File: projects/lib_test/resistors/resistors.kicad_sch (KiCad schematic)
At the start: 0 parts

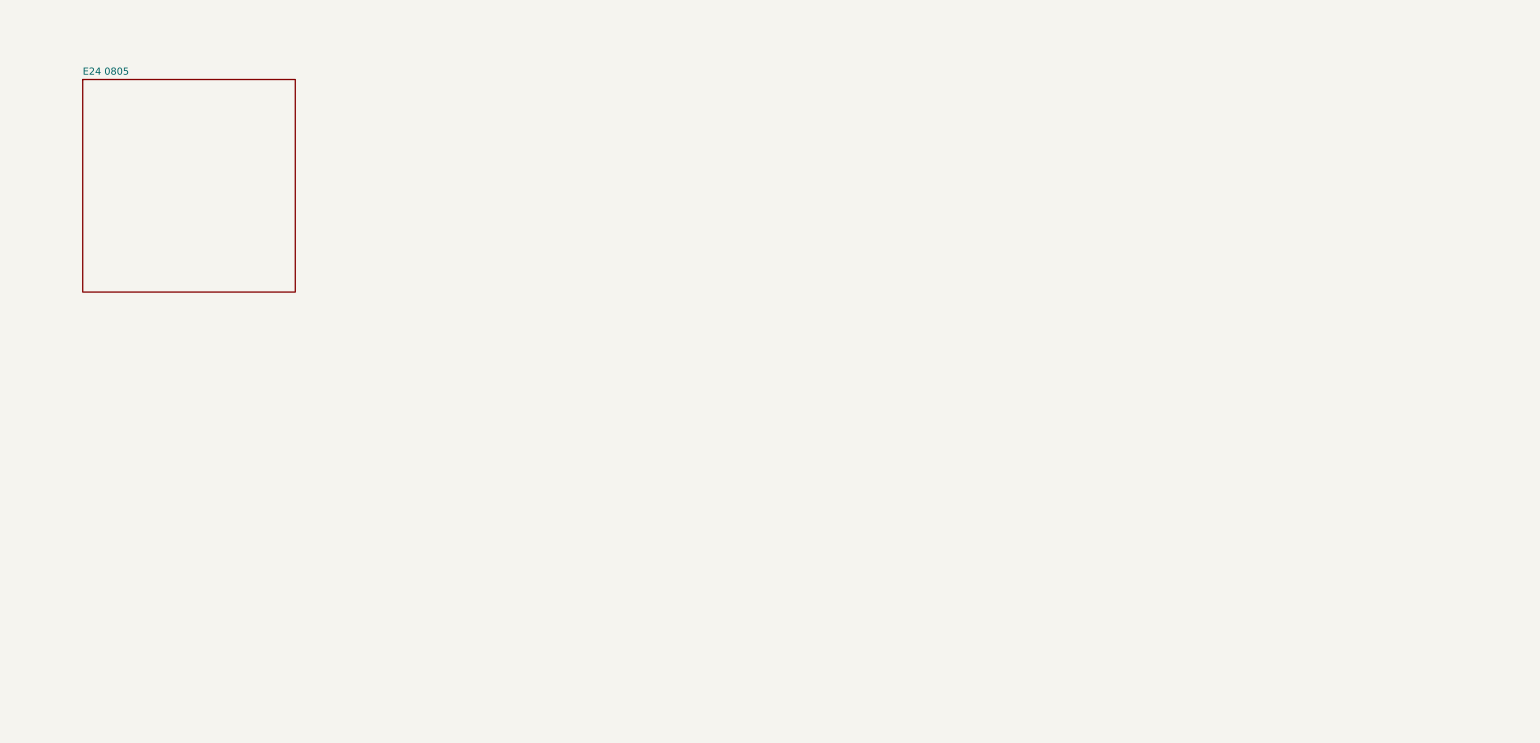
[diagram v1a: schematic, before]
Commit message: put all symbols in the test designs
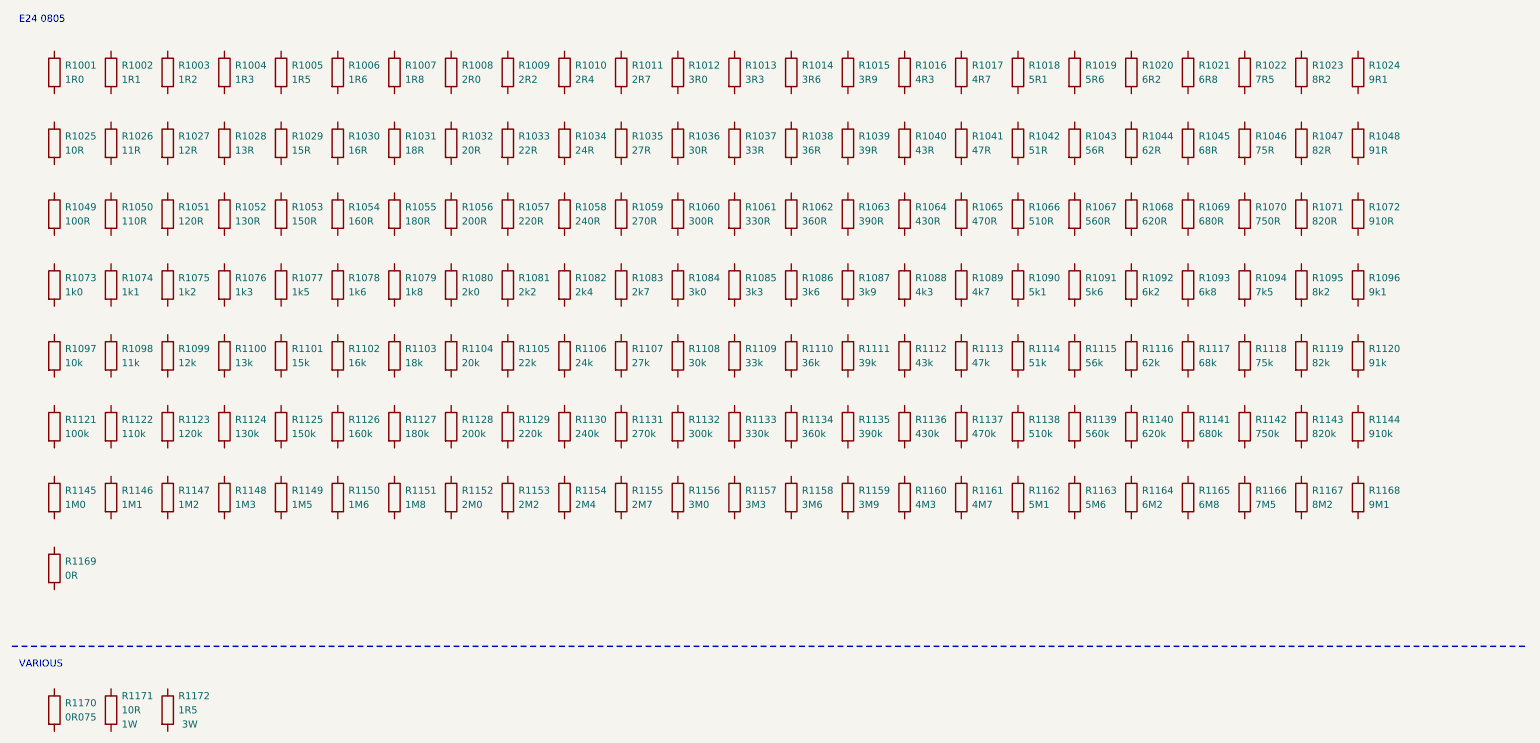
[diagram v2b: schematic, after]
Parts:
- added R1001: 1R0, lily_footprints:res_0805, symbol lily_symbols:res_1R0_1%_125mW_0805
- added R1002: 1R1, lily_footprints:res_0805, symbol lily_symbols:res_1R1_1%_125mW_0805
- added R1003: 1R2, lily_footprints:res_0805, symbol lily_symbols:res_1R2_1%_125mW_0805
- added R1004: 1R3, lily_footprints:res_0805, symbol lily_symbols:res_1R3_1%_125mW_0805
- added R1005: 1R5, lily_footprints:res_0805, symbol lily_symbols:res_1R5_1%_125mW_0805
- added R1006: 1R6, lily_footprints:res_0805, symbol lily_symbols:res_1R6_1%_125mW_0805
- added R1007: 1R8, lily_footprints:res_0805, symbol lily_symbols:res_1R8_1%_125mW_0805
- added R1008: 2R0, lily_footprints:res_0805, symbol lily_symbols:res_2R0_1%_125mW_0805
- added R1009: 2R2, lily_footprints:res_0805, symbol lily_symbols:res_2R2_1%_125mW_0805
- added R1010: 2R4, lily_footprints:res_0805, symbol lily_symbols:res_2R4_1%_125mW_0805
- added R1011: 2R7, lily_footprints:res_0805, symbol lily_symbols:res_2R7_1%_125mW_0805
- added R1012: 3R0, lily_footprints:res_0805, symbol lily_symbols:res_3R0_1%_125mW_0805
- added R1013: 3R3, lily_footprints:res_0805, symbol lily_symbols:res_3R3_1%_125mW_0805
- added R1014: 3R6, lily_footprints:res_0805, symbol lily_symbols:res_3R6_1%_125mW_0805
- added R1015: 3R9, lily_footprints:res_0805, symbol lily_symbols:res_3R9_1%_125mW_0805
- added R1016: 4R3, lily_footprints:res_0805, symbol lily_symbols:res_4R3_1%_125mW_0805
- added R1017: 4R7, lily_footprints:res_0805, symbol lily_symbols:res_4R7_1%_125mW_0805
- added R1018: 5R1, lily_footprints:res_0805, symbol lily_symbols:res_5R1_1%_125mW_0805
- added R1019: 5R6, lily_footprints:res_0805, symbol lily_symbols:res_5R6_1%_125mW_0805
- added R1020: 6R2, lily_footprints:res_0805, symbol lily_symbols:res_6R2_1%_125mW_0805
- added R1021: 6R8, lily_footprints:res_0805, symbol lily_symbols:res_6R8_1%_125mW_0805
- added R1022: 7R5, lily_footprints:res_0805, symbol lily_symbols:res_7R5_1%_125mW_0805
- added R1023: 8R2, lily_footprints:res_0805, symbol lily_symbols:res_8R2_1%_125mW_0805
- added R1024: 9R1, lily_footprints:res_0805, symbol lily_symbols:res_9R1_1%_125mW_0805
- added R1025: 10R, lily_footprints:res_0805, symbol lily_symbols:res_10R_1%_125mW_0805
- added R1026: 11R, lily_footprints:res_0805, symbol lily_symbols:res_11R_1%_125mW_0805
- added R1027: 12R, lily_footprints:res_0805, symbol lily_symbols:res_12R_1%_125mW_0805
- added R1028: 13R, lily_footprints:res_0805, symbol lily_symbols:res_13R_1%_125mW_0805
- added R1029: 15R, lily_footprints:res_0805, symbol lily_symbols:res_15R_1%_125mW_0805
- added R1030: 16R, lily_footprints:res_0805, symbol lily_symbols:res_16R_1%_125mW_0805
- added R1031: 18R, lily_footprints:res_0805, symbol lily_symbols:res_18R_1%_125mW_0805
- added R1032: 20R, lily_footprints:res_0805, symbol lily_symbols:res_20R_1%_125mW_0805
- added R1033: 22R, lily_footprints:res_0805, symbol lily_symbols:res_22R_1%_125mW_0805
- added R1034: 24R, lily_footprints:res_0805, symbol lily_symbols:res_24R_1%_125mW_0805
- added R1035: 27R, lily_footprints:res_0805, symbol lily_symbols:res_27R_1%_125mW_0805
- added R1036: 30R, lily_footprints:res_0805, symbol lily_symbols:res_30R_1%_125mW_0805
- added R1037: 33R, lily_footprints:res_0805, symbol lily_symbols:res_33R_1%_125mW_0805
- added R1038: 36R, lily_footprints:res_0805, symbol lily_symbols:res_36R_1%_125mW_0805
- added R1039: 39R, lily_footprints:res_0805, symbol lily_symbols:res_39R_1%_125mW_0805
- added R1040: 43R, lily_footprints:res_0805, symbol lily_symbols:res_43R_1%_125mW_0805
- added R1041: 47R, lily_footprints:res_0805, symbol lily_symbols:res_47R_1%_125mW_0805
- added R1042: 51R, lily_footprints:res_0805, symbol lily_symbols:res_51R_1%_125mW_0805
- added R1043: 56R, lily_footprints:res_0805, symbol lily_symbols:res_56R_1%_125mW_0805
- added R1044: 62R, lily_footprints:res_0805, symbol lily_symbols:res_62R_1%_125mW_0805
- added R1045: 68R, lily_footprints:res_0805, symbol lily_symbols:res_68R_1%_125mW_0805
- added R1046: 75R, lily_footprints:res_0805, symbol lily_symbols:res_75R_1%_125mW_0805
- added R1047: 82R, lily_footprints:res_0805, symbol lily_symbols:res_82R_1%_125mW_0805
- added R1048: 91R, lily_footprints:res_0805, symbol lily_symbols:res_91R_1%_125mW_0805
- added R1049: 100R, lily_footprints:res_0805, symbol lily_symbols:res_100R_1%_125mW_0805
- added R1050: 110R, lily_footprints:res_0805, symbol lily_symbols:res_110R_1%_125mW_0805
- added R1051: 120R, lily_footprints:res_0805, symbol lily_symbols:res_120R_1%_125mW_0805
- added R1052: 130R, lily_footprints:res_0805, symbol lily_symbols:res_130R_1%_125mW_0805
- added R1053: 150R, lily_footprints:res_0805, symbol lily_symbols:res_150R_1%_125mW_0805
- added R1054: 160R, lily_footprints:res_0805, symbol lily_symbols:res_160R_1%_125mW_0805
- added R1055: 180R, lily_footprints:res_0805, symbol lily_symbols:res_180R_1%_125mW_0805
- added R1056: 200R, lily_footprints:res_0805, symbol lily_symbols:res_200R_1%_125mW_0805
- added R1057: 220R, lily_footprints:res_0805, symbol lily_symbols:res_220R_1%_125mW_0805
- added R1058: 240R, lily_footprints:res_0805, symbol lily_symbols:res_240R_1%_125mW_0805
- added R1059: 270R, lily_footprints:res_0805, symbol lily_symbols:res_270R_1%_125mW_0805
- added R1060: 300R, lily_footprints:res_0805, symbol lily_symbols:res_300R_1%_125mW_0805
- added R1061: 330R, lily_footprints:res_0805, symbol lily_symbols:res_330R_1%_125mW_0805
- added R1062: 360R, lily_footprints:res_0805, symbol lily_symbols:res_360R_1%_125mW_0805
- added R1063: 390R, lily_footprints:res_0805, symbol lily_symbols:res_390R_1%_125mW_0805
- added R1064: 430R, lily_footprints:res_0805, symbol lily_symbols:res_430R_1%_125mW_0805
- added R1065: 470R, lily_footprints:res_0805, symbol lily_symbols:res_470R_1%_125mW_0805
- added R1066: 510R, lily_footprints:res_0805, symbol lily_symbols:res_510R_1%_125mW_0805
- added R1067: 560R, lily_footprints:res_0805, symbol lily_symbols:res_560R_1%_125mW_0805
- added R1068: 620R, lily_footprints:res_0805, symbol lily_symbols:res_620R_1%_125mW_0805
- added R1069: 680R, lily_footprints:res_0805, symbol lily_symbols:res_680R_1%_125mW_0805
- added R1070: 750R, lily_footprints:res_0805, symbol lily_symbols:res_750R_1%_125mW_0805
- added R1071: 820R, lily_footprints:res_0805, symbol lily_symbols:res_820R_1%_125mW_0805
- added R1072: 910R, lily_footprints:res_0805, symbol lily_symbols:res_910R_1%_125mW_0805
- added R1073: 1k0, lily_footprints:res_0805, symbol lily_symbols:res_1k0_1%_125mW_0805
- added R1074: 1k1, lily_footprints:res_0805, symbol lily_symbols:res_1k1_1%_125mW_0805
- added R1075: 1k2, lily_footprints:res_0805, symbol lily_symbols:res_1k2_1%_125mW_0805
- added R1076: 1k3, lily_footprints:res_0805, symbol lily_symbols:res_1k3_1%_125mW_0805
- added R1077: 1k5, lily_footprints:res_0805, symbol lily_symbols:res_1k5_1%_125mW_0805
- added R1078: 1k6, lily_footprints:res_0805, symbol lily_symbols:res_1k6_1%_125mW_0805
- added R1079: 1k8, lily_footprints:res_0805, symbol lily_symbols:res_1k8_1%_125mW_0805
- added R1080: 2k0, lily_footprints:res_0805, symbol lily_symbols:res_2k0_1%_125mW_0805
- added R1081: 2k2, lily_footprints:res_0805, symbol lily_symbols:res_2k2_1%_125mW_0805
- added R1082: 2k4, lily_footprints:res_0805, symbol lily_symbols:res_2k4_1%_125mW_0805
- added R1083: 2k7, lily_footprints:res_0805, symbol lily_symbols:res_2k7_1%_125mW_0805
- added R1084: 3k0, lily_footprints:res_0805, symbol lily_symbols:res_3k0_1%_125mW_0805
- added R1085: 3k3, lily_footprints:res_0805, symbol lily_symbols:res_3k3_1%_125mW_0805
- added R1086: 3k6, lily_footprints:res_0805, symbol lily_symbols:res_3k6_1%_125mW_0805
- added R1087: 3k9, lily_footprints:res_0805, symbol lily_symbols:res_3k9_1%_125mW_0805
- added R1088: 4k3, lily_footprints:res_0805, symbol lily_symbols:res_4k3_1%_125mW_0805
- added R1089: 4k7, lily_footprints:res_0805, symbol lily_symbols:res_4k7_1%_125mW_0805
- added R1090: 5k1, lily_footprints:res_0805, symbol lily_symbols:res_5k1_1%_125mW_0805
- added R1091: 5k6, lily_footprints:res_0805, symbol lily_symbols:res_5k6_1%_125mW_0805
- added R1092: 6k2, lily_footprints:res_0805, symbol lily_symbols:res_6k2_1%_125mW_0805
- added R1093: 6k8, lily_footprints:res_0805, symbol lily_symbols:res_6k8_1%_125mW_0805
- added R1094: 7k5, lily_footprints:res_0805, symbol lily_symbols:res_7k5_1%_125mW_0805
- added R1095: 8k2, lily_footprints:res_0805, symbol lily_symbols:res_8k2_1%_125mW_0805
- added R1096: 9k1, lily_footprints:res_0805, symbol lily_symbols:res_9k1_1%_125mW_0805
- added R1097: 10k, lily_footprints:res_0805, symbol lily_symbols:res_10k_1%_125mW_0805
- added R1098: 11k, lily_footprints:res_0805, symbol lily_symbols:res_11k_1%_125mW_0805
- added R1099: 12k, lily_footprints:res_0805, symbol lily_symbols:res_12k_1%_125mW_0805
- added R1100: 13k, lily_footprints:res_0805, symbol lily_symbols:res_13k_1%_125mW_0805
- added R1101: 15k, lily_footprints:res_0805, symbol lily_symbols:res_15k_1%_125mW_0805
- added R1102: 16k, lily_footprints:res_0805, symbol lily_symbols:res_16k_1%_125mW_0805
- added R1103: 18k, lily_footprints:res_0805, symbol lily_symbols:res_18k_1%_125mW_0805
- added R1104: 20k, lily_footprints:res_0805, symbol lily_symbols:res_20k_1%_125mW_0805
- added R1105: 22k, lily_footprints:res_0805, symbol lily_symbols:res_22k_1%_125mW_0805
- added R1106: 24k, lily_footprints:res_0805, symbol lily_symbols:res_24k_1%_125mW_0805
- added R1107: 27k, lily_footprints:res_0805, symbol lily_symbols:res_27k_1%_125mW_0805
- added R1108: 30k, lily_footprints:res_0805, symbol lily_symbols:res_30k_1%_125mW_0805
- added R1109: 33k, lily_footprints:res_0805, symbol lily_symbols:res_33k_1%_125mW_0805
- added R1110: 36k, lily_footprints:res_0805, symbol lily_symbols:res_36k_1%_125mW_0805
- added R1111: 39k, lily_footprints:res_0805, symbol lily_symbols:res_39k_1%_125mW_0805
- added R1112: 43k, lily_footprints:res_0805, symbol lily_symbols:res_43k_1%_125mW_0805
- added R1113: 47k, lily_footprints:res_0805, symbol lily_symbols:res_47k_1%_125mW_0805
- added R1114: 51k, lily_footprints:res_0805, symbol lily_symbols:res_51k_1%_125mW_0805
- added R1115: 56k, lily_footprints:res_0805, symbol lily_symbols:res_56k_1%_125mW_0805
- added R1116: 62k, lily_footprints:res_0805, symbol lily_symbols:res_62k_1%_125mW_0805
- added R1117: 68k, lily_footprints:res_0805, symbol lily_symbols:res_68k_1%_125mW_0805
- added R1118: 75k, lily_footprints:res_0805, symbol lily_symbols:res_75k_1%_125mW_0805
- added R1119: 82k, lily_footprints:res_0805, symbol lily_symbols:res_82k_1%_125mW_0805
- added R1120: 91k, lily_footprints:res_0805, symbol lily_symbols:res_91k_1%_125mW_0805
- added R1121: 100k, lily_footprints:res_0805, symbol lily_symbols:res_100k_1%_125mW_0805
- added R1122: 110k, lily_footprints:res_0805, symbol lily_symbols:res_110k_1%_125mW_0805
- added R1123: 120k, lily_footprints:res_0805, symbol lily_symbols:res_120k_1%_125mW_0805
- added R1124: 130k, lily_footprints:res_0805, symbol lily_symbols:res_130k_1%_125mW_0805
- added R1125: 150k, lily_footprints:res_0805, symbol lily_symbols:res_150k_1%_125mW_0805
- added R1126: 160k, lily_footprints:res_0805, symbol lily_symbols:res_160k_1%_125mW_0805
- added R1127: 180k, lily_footprints:res_0805, symbol lily_symbols:res_180k_1%_125mW_0805
- added R1128: 200k, lily_footprints:res_0805, symbol lily_symbols:res_200k_1%_125mW_0805
- added R1129: 220k, lily_footprints:res_0805, symbol lily_symbols:res_220k_1%_125mW_0805
- added R1130: 240k, lily_footprints:res_0805, symbol lily_symbols:res_240k_1%_125mW_0805
- added R1131: 270k, lily_footprints:res_0805, symbol lily_symbols:res_270k_1%_125mW_0805
- added R1132: 300k, lily_footprints:res_0805, symbol lily_symbols:res_300k_1%_125mW_0805
- added R1133: 330k, lily_footprints:res_0805, symbol lily_symbols:res_330k_1%_125mW_0805
- added R1134: 360k, lily_footprints:res_0805, symbol lily_symbols:res_360k_1%_125mW_0805
- added R1135: 390k, lily_footprints:res_0805, symbol lily_symbols:res_390k_1%_125mW_0805
- added R1136: 430k, lily_footprints:res_0805, symbol lily_symbols:res_430k_1%_125mW_0805
- added R1137: 470k, lily_footprints:res_0805, symbol lily_symbols:res_470k_1%_125mW_0805
- added R1138: 510k, lily_footprints:res_0805, symbol lily_symbols:res_510k_1%_125mW_0805
- added R1139: 560k, lily_footprints:res_0805, symbol lily_symbols:res_560k_1%_125mW_0805
- added R1140: 620k, lily_footprints:res_0805, symbol lily_symbols:res_620k_1%_125mW_0805
- added R1141: 680k, lily_footprints:res_0805, symbol lily_symbols:res_680k_1%_125mW_0805
- added R1142: 750k, lily_footprints:res_0805, symbol lily_symbols:res_750k_1%_125mW_0805
- added R1143: 820k, lily_footprints:res_0805, symbol lily_symbols:res_820k_1%_125mW_0805
- added R1144: 910k, lily_footprints:res_0805, symbol lily_symbols:res_910k_1%_125mW_0805
- added R1145: 1M0, lily_footprints:res_0805, symbol lily_symbols:res_1M0_1%_125mW_0805
- added R1146: 1M1, lily_footprints:res_0805, symbol lily_symbols:res_1M1_1%_125mW_0805
- added R1147: 1M2, lily_footprints:res_0805, symbol lily_symbols:res_1M2_1%_125mW_0805
- added R1148: 1M3, lily_footprints:res_0805, symbol lily_symbols:res_1M3_1%_125mW_0805
- added R1149: 1M5, lily_footprints:res_0805, symbol lily_symbols:res_1M5_1%_125mW_0805
- added R1150: 1M6, lily_footprints:res_0805, symbol lily_symbols:res_1M6_1%_125mW_0805
- added R1151: 1M8, lily_footprints:res_0805, symbol lily_symbols:res_1M8_1%_125mW_0805
- added R1152: 2M0, lily_footprints:res_0805, symbol lily_symbols:res_2M0_1%_125mW_0805
- added R1153: 2M2, lily_footprints:res_0805, symbol lily_symbols:res_2M2_1%_125mW_0805
- added R1154: 2M4, lily_footprints:res_0805, symbol lily_symbols:res_2M4_1%_125mW_0805
- added R1155: 2M7, lily_footprints:res_0805, symbol lily_symbols:res_2M7_1%_125mW_0805
- added R1156: 3M0, lily_footprints:res_0805, symbol lily_symbols:res_3M0_1%_125mW_0805
- added R1157: 3M3, lily_footprints:res_0805, symbol lily_symbols:res_3M3_1%_125mW_0805
- added R1158: 3M6, lily_footprints:res_0805, symbol lily_symbols:res_3M6_1%_125mW_0805
- added R1159: 3M9, lily_footprints:res_0805, symbol lily_symbols:res_3M9_1%_125mW_0805
- added R1160: 4M3, lily_footprints:res_0805, symbol lily_symbols:res_4M3_1%_125mW_0805
- added R1161: 4M7, lily_footprints:res_0805, symbol lily_symbols:res_4M7_1%_125mW_0805
- added R1162: 5M1, lily_footprints:res_0805, symbol lily_symbols:res_5M1_1%_125mW_0805
- added R1163: 5M6, lily_footprints:res_0805, symbol lily_symbols:res_5M6_1%_125mW_0805
- added R1164: 6M2, lily_footprints:res_0805, symbol lily_symbols:res_6M2_1%_125mW_0805
- added R1165: 6M8, lily_footprints:res_0805, symbol lily_symbols:res_6M8_1%_125mW_0805
- added R1166: 7M5, lily_footprints:res_0805, symbol lily_symbols:res_7M5_1%_125mW_0805
- added R1167: 8M2, lily_footprints:res_0805, symbol lily_symbols:res_8M2_1%_125mW_0805
- added R1168: 9M1, lily_footprints:res_0805, symbol lily_symbols:res_9M1_1%_125mW_0805
- added R1169: 0R, lily_footprints:res_0805, symbol lily_symbols:res_0R_1%_125mW_0805
- added R1170: 0R075, lily_footprints:res_2512, symbol lily_symbols:res_0R075_1%_2W_2512
- added R1171: 10R, lily_footprints:res_2512, symbol lily_symbols:res_10R_1%_1W_2512
- added R1172: 1R5, lily_footprints:res_2512, symbol lily_symbols:res_1R5_1%_3W_2512
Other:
- removed sheet E24 0805
- note added: "E24 0805"
- note added: "VARIOUS"
